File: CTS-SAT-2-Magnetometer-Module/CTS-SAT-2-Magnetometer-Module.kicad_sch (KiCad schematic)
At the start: 24 parts, among them J1 PicoBlade, J2 SWD, U1 MMC5983MA, U2 LIS2MDL, U3 STM32F072C8Tx, U4 MIC5365-3.3YD5

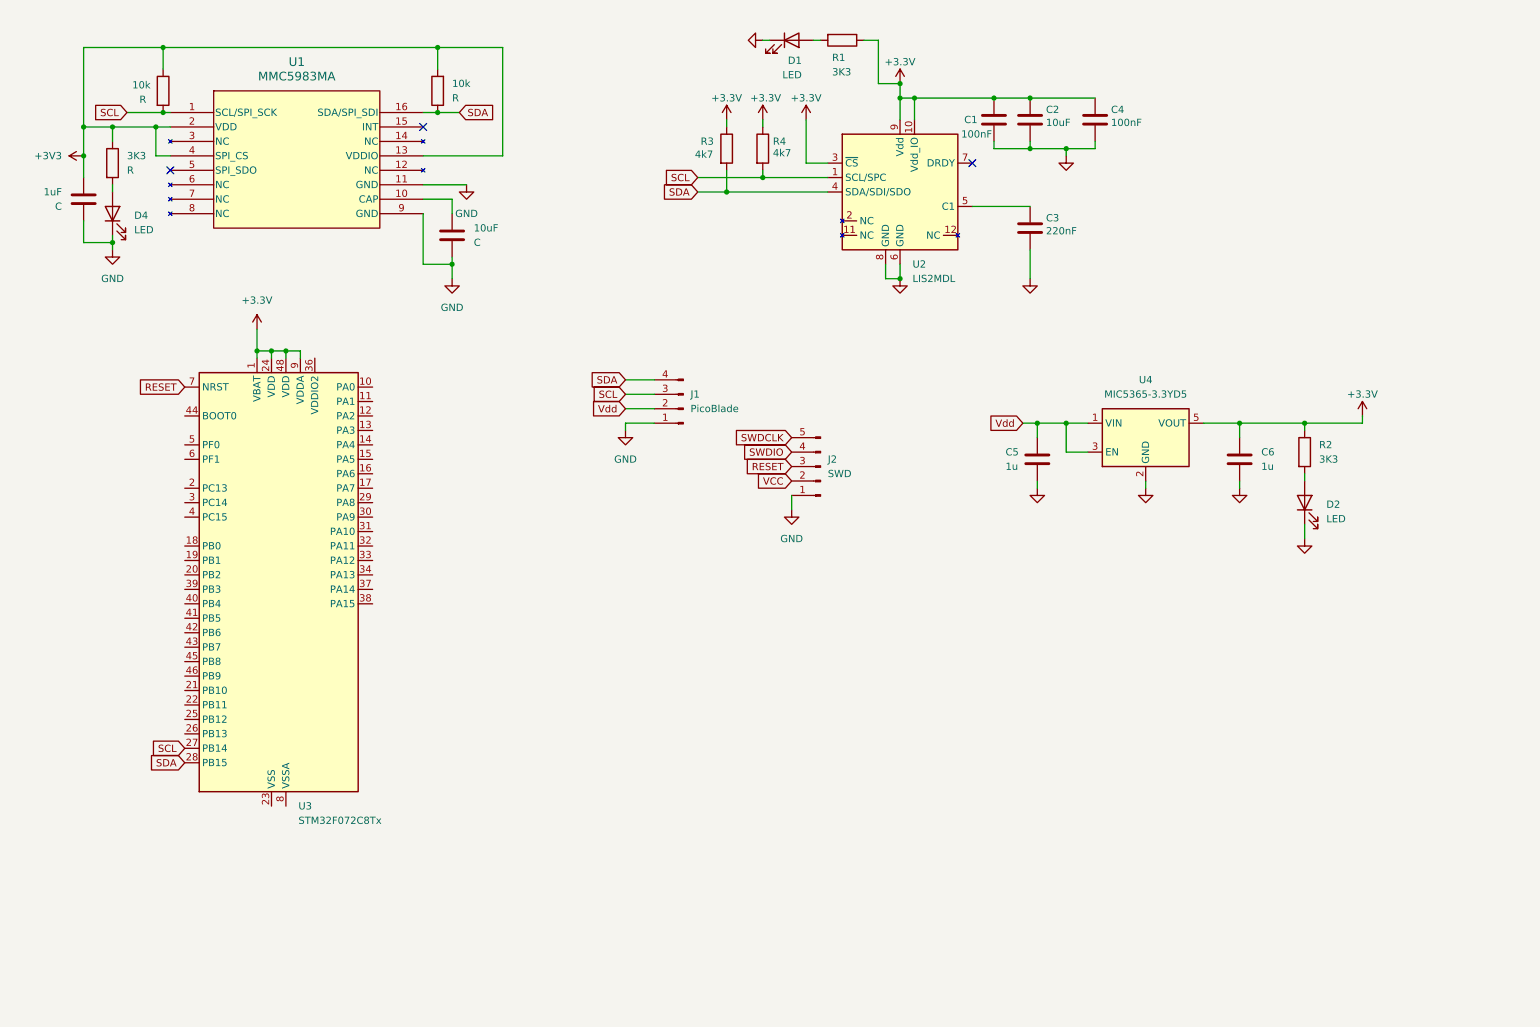
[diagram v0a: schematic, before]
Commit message: Updated Schematic and Started Layout
Assigned Footprints and Started PCB layout
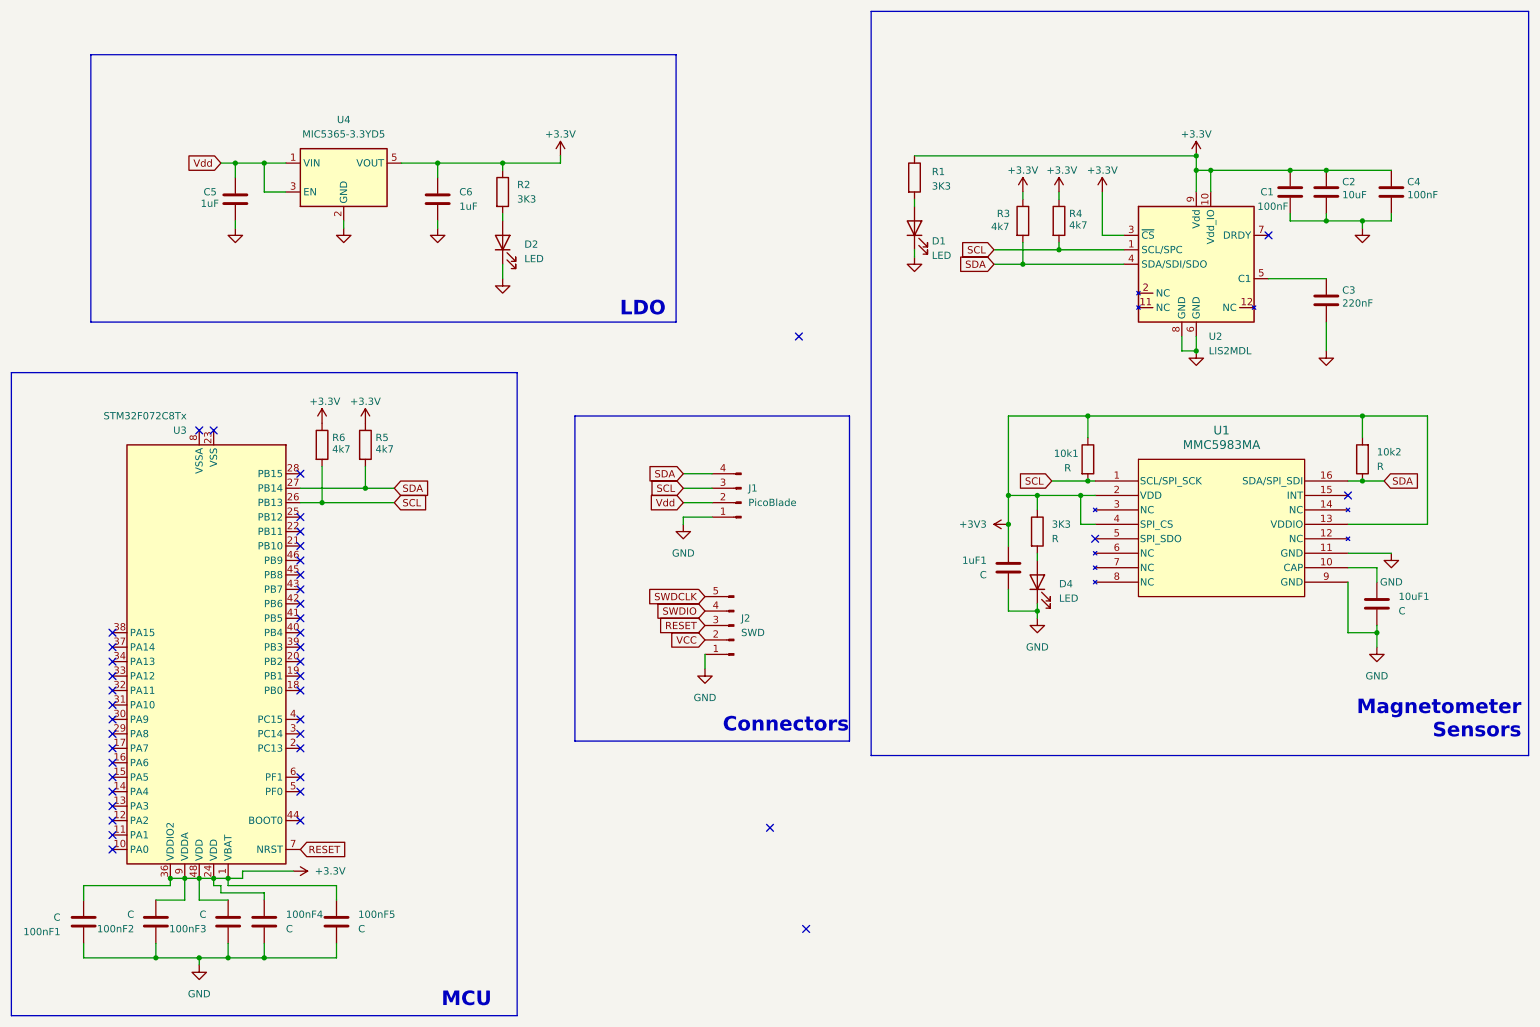
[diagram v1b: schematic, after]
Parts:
- added 100nF1, 100nF2, 100nF3, 100nF4, 100nF5: C, Capacitor_SMD:C_0603_1608Metric_Pad1.08x0.95mm_HandSolder, symbol Device:C
- added R5, R6: 4k7, Resistor_SMD:R_0603_1608Metric_Pad0.98x0.95mm_HandSolder, symbol Device:R
- 10k1, 10k2: renamed from 10k; footprint (none) -> Resistor_SMD:R_0603_1608Metric_Pad0.98x0.95mm_HandSolder
- 10uF1: renamed from 10uF; footprint (none) -> Capacitor_SMD:C_0603_1608Metric_Pad1.08x0.95mm_HandSolder
- 1uF1: renamed from 1uF; footprint (none) -> Capacitor_SMD:C_0603_1608Metric_Pad1.08x0.95mm_HandSolder
- 3K3: footprint (none) -> Resistor_SMD:R_0603_1608Metric_Pad0.98x0.95mm_HandSolder
- C5, C6: value 1u -> 1uF
- D4: footprint (none) -> LED_SMD:LED_0603_1608Metric_Pad1.05x0.95mm_HandSolder
- J2: footprint (none) -> Connector_PinSocket_2.54mm:PinSocket_1x06_P2.54mm_Vertical
- U1: footprint MMC5983MA_MEM -> 00_Footprint_Library:MMC5983MA_MEM
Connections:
- net +3.3V: now also U3.36 (VDDIO2), 100nF1.2, 100nF2.2, 100nF3.2, 100nF4.2, 100nF5.1, R5.1, R6.1
- net GND: now also 100nF1.1, 100nF2.1, 100nF3.1, 100nF4.1, 100nF5.2
- net SCL: now also U3.26 (PB13), R6.2; no longer U3.27 (PB14)
- net SDA: now also U3.27 (PB14), R5.2; no longer U3.28 (PB15)
- no-connect marks 3 -> 44
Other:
- note added: "Connectors"
- note added: "LDO"
- note added: "MCU"
- note added: "Magnetometer Sensors"
- moved on the sheet: 10k1, 10k2, 10uF1, 1uF1, 3K3, C1, C2, C3, C4, C5, C6, D1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

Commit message: Started PCB Routing
Still need to figure out how to do routing for communication lines
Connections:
- net +3V3 is gone; now on net +3.3V: 10k1.1, 10k2.2, 1uF1.1, 3K3.1, U1.13 (VDDIO), U1.2 (VDD), U1.4 (SPI_CS)
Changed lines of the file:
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@@
 	(wire
 		(pts
-			(xy 57.15 168.91) (xy 57.15 170.18)
-		)
-		(stroke
-			(width 0)
-			(type default)
-		)
-	)
-	(wire
-		(pts
 			(xy 113.03 43.18) (xy 113.03 44.45)
 		)
@@
 	(wire
 		(pts
-			(xy 66.04 168.91) (xy 57.15 168.91)
+			(xy 185.42 105.41) (xy 185.42 107.95)
 		)
 		(stroke
@@
 	(wire
 		(pts
+			(xy 185.42 107.95) (xy 191.77 107.95)
+		)
+		(stroke
+			(width 0)
+			(type default)
+		)
+	)
+	(wire
+		(pts
 			(xy 200.66 50.8) (xy 200.66 49.53)
 		)
@@
 	(wire
 		(pts
-			(xy 57.15 170.18) (xy 54.61 170.18)
+			(xy 54.61 170.18) (xy 77.47 170.18)
 		)
 		(stroke
@@
 	)
 	(symbol
+		(lib_id "power:+3.3V")
+		(at 185.42 105.41 0)
+		(unit 1)
+		(exclude_from_sim no)
+		(in_bom yes)
+		(on_board yes)
+		(dnp no)
+		(property "Reference" "#PWR01"
+			(at 185.42 109.22 0)
+			(effects
+				(font
+					(size 1.27 1.27)
+				)
+				(hide yes)
+			)
+		)
+		(property "Value" "+3.3V"
+			(at 185.42 101.6 0)
+			(effects
+				(font
+					(size 1.27 1.27)
+				)
+			)
+		)
+		(property "Footprint" ""
+			(at 185.42 105.41 0)
+			(effects
+				(font
+					(size 1.27 1.27)
+				)
+				(hide yes)
+			)
+		)
+		(property "Datasheet" ""
+			(at 185.42 105.41 0)
+			(effects
+				(font
+					(size 1.27 1.27)
+				)
+				(hide yes)
+			)
+		)
+		(property "Description" "Power symbol creates a global label with name \"+3.3V\""
+			(at 185.42 105.41 0)
+			(effects
+				(font
+					(size 1.27 1.27)
+				)
+				(hide yes)
+			)
+		)
+		(pin "1"
+		)
+		(instances
+			(project "CTS-SAT-2-Magnetometer-Module"
+				(path "/c009ac64-8176-4e92-bfe3-b763ec3b9dfb"
+					(reference "#PWR01")
+					(unit 1)
+				)
+			)
+		)
+	)
+	(symbol
 		(lib_id "power:GND")
 		(at 138.43 133.35 0)
@@
 	(symbol
 		(lib_id "power:+3.3V")
-		(at 66.04 168.91 270)
+		(at 77.47 170.18 0)
 		(unit 1)
 		(exclude_from_sim no)
@@
 		(fields_autoplaced yes)
 		(property "Reference" "#PWR027"
-			(at 62.23 168.91 0)
+			(at 77.47 173.99 0)
 			(effects
 				(font
@@
 		)
 		(property "Value" "+3.3V"
-			(at 69.85 168.9101 90)
+			(at 80.01 168.9099 0)
 			(effects
 				(font
@@
 		)
 		(property "Footprint" ""
-			(at 66.04 168.91 0)
+			(at 77.47 170.18 0)
 			(effects
 				(font
@@
 		)
 		(property "Datasheet" ""
-			(at 66.04 168.91 0)
+			(at 77.47 170.18 0)
 			(effects
 				(font
@@
 		)
 		(property "Description" "Power symbol creates a global label with name \"+3.3V\""
-			(at 66.04 168.91 0)
+			(at 77.47 170.18 0)
 			(effects
 				(font
@@
 					(unit 1)
 				)
-			)
-		)
-	)
-	(symbol
-		(lib_id "power:+3V3")
-		(at 191.77 107.95 90)
-		(unit 1)
-		(exclude_from_sim no)
-		(in_bom yes)
-		(on_board yes)
-		(dnp no)
-		(fields_autoplaced yes)
-		(property "Reference" "#PWR01"
-			(at 195.58 107.95 0)
-			(effects
-				(font
-					(size 1.27 1.27)
-				)
-				(hide yes)
-			)
-		)
-		(property "Value" "+3V3"
-			(at 187.96 107.9499 90)
-			(effects
-				(font
-					(size 1.27 1.27)
-				)
-				(justify left)
-			)
-		)
-		(property "Footprint" ""
-			(at 191.77 107.95 0)
-			(effects
-				(font
-					(size 1.27 1.27)
-				)
-				(hide yes)
-			)
-		)
-		(property "Datasheet" ""
-			(at 191.77 107.95 0)
-			(effects
-				(font
-					(size 1.27 1.27)
-				)
-				(hide yes)
-			)
-		)
-		(property "Description" "Power symbol creates a global label with name \"+3V3\""
-			(at 191.77 107.95 0)
-			(effects
-				(font
-					(size 1.27 1.27)
-				)
-				(hide yes)
-			)
-		)
-		(pin "1"
-		)
-		(instances
-			(project ""
-				(path "/c009ac64-8176-4e92-bfe3-b763ec3b9dfb"
-					(reference "#PWR01")
-					(unit 1)
-				)

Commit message: Changed one of the footprints
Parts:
- J2: footprint Connector_PinSocket_2.54mm:PinSocket_1x06_P2.54mm_Vertical -> Connector_PinSocket_2.54mm:PinSocket_1x05_P2.54mm_Vertical
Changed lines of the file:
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@@
 			)
 		)
-		(property "Footprint" "Connector_PinSocket_2.54mm:PinSocket_1x06_P2.54mm_Vertical"
+		(property "Footprint" "Connector_PinSocket_2.54mm:PinSocket_1x05_P2.54mm_Vertical"
 			(at 143.51 125.73 0)
 			(effects

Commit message: Few first edits
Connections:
- net VCC is gone; now on net Vdd: J2.2 (Pin_2)
- net +3.3V: no longer 10k1.1, 10k2.2, 1uF1.1, 3K3.1, U1.13 (VDDIO), U1.2 (VDD), U1.4 (SPI_CS)
- new net +3V0: 10k1.1, 10k2.2, 1uF1.1, 3K3.1, U1.13 (VDDIO), U1.2 (VDD), U1.4 (SPI_CS)

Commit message: Aaryan's Changes applied
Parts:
- removed 10k1, 10k2, 3K3: R, Resistor_SMD:R_0603_1608Metric_Pad0.98x0.95mm_HandSolder, symbol Device:R
- removed D1: LED, LED_SMD:LED_0603_1608Metric_Pad1.05x0.95mm_HandSolder, symbol Device:LED
- added C7: 100nF, symbol Device:C
- added D3: LED, LED_SMD:LED_0603_1608Metric_Pad1.05x0.95mm_HandSolder, symbol Device:LED
- added R7: 3K3, Resistor_SMD:R_0603_1608Metric_Pad0.98x0.95mm_HandSolder, symbol Device:R
- added SW1: SW_Push, symbol Switch:SW_Push
- C: renamed from 100nF3; value C -> 100nF3
- C: renamed from 100nF4; value C -> 100nF4
- C: renamed from 100nF1; value C -> 100nF1
- C: renamed from 100nF5; value C -> 100nF5
- C: renamed from 10uF1; value C -> 10uF1
- C: renamed from 100nF2; value C -> 100nF2
- C: renamed from 1uF1; value C -> 1uF1
- R1: value 3K3 -> 0; footprint Resistor_SMD:R_0603_1608Metric_Pad0.98x0.95mm_HandSolder -> (none)
- R3: value 4k7 -> 10k; footprint Resistor_SMD:R_0603_1608Metric_Pad0.98x0.95mm_HandSolder -> (none)
- R4: value 4k7 -> 3K3
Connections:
- net +3V0: now also C.1, C.2, C.2, C.2, C.2, C1.2, C2.1, C4.1, C6.1, R1.1, R2.1, R3.1, R5.1, R6.1, U2.10 (Vdd_IO), U2.9 (Vdd), U3.1 (VBAT), U3.24 (VDD), U3.36 (VDDIO2), U3.48 (VDD), U3.9 (VDDA), U4.5 (VOUT)
- net GND: now also U3.23 (VSS), U3.35 (VSS), U3.47 (VSS), U3.8 (VSSA), C7.2, D3.1 (K), SW1.2
- net SCL: no longer R4.2
- net SDA: no longer R3.2
- net SWDCLK: now also U3.37 (PA14)
- net SWDIO: now also U3.34 (PA13)
- net at U3.18 (PB0): now also R4.1
- net at U3.19 (PB1): now also R7.1
- net DRDY: now reaches U3.21 (PB10)
- net DRDY: now also U2.7 (DRDY)
- net at R1.2: now also U2.3 (~{CS})
- net at D4.2 (A): now also R7.2
- removed net +3.3V: C.1, C.2, C.2, C.2, C.2, C1.2, C2.1, C4.1, C6.1, R1.1, R2.1, R3.1, R4.1, R5.1, R6.1, U2.10 (Vdd_IO), U2.3 (~{CS}), U2.9 (Vdd), U3.1 (VBAT), U3.24 (VDD), U3.36 (VDDIO2), U3.48 (VDD), U3.9 (VDDA), U4.5 (VOUT)
- net RESET renamed NRST
- net NRST: now also R3.2, C7.1, SW1.1
- new net: D3.2 (A), R4.2
- no-connect marks 44 -> 33
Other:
- moved on the sheet: C, C5, C6, D2, R2, R5, R6, U3, U4

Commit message: Final changes for Aaryan
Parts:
- removed J1: PicoBlade, Connector_PinHeader_2.54mm:PinHeader_1x04_P2.54mm_Vertical, symbol Connector:Conn_01x04_Pin
- added J3: SWD, Connector_PinHeader_2.54mm:PinHeader_1x05_P2.54mm_Vertical, symbol Connector:Conn_01x05_Pin
- C7: footprint (none) -> Capacitor_SMD:C_0603_1608Metric_Pad1.08x0.95mm_HandSolder
- R1, R3: footprint (none) -> Resistor_SMD:R_0603_1608Metric_Pad0.98x0.95mm_HandSolder
- SW1: footprint (none) -> Button_Switch_SMD:SW_SPST_EVQP0
- renumbered C to C10, C to C11, C to C12, C to C13, C to C14, C to C8, C to C9
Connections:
- net GND: now also J3.1 (Pin_1)
- net NRST: now also J3.3 (Pin_3)
- net SWDCLK: now also J3.5 (Pin_5)
- net SWDIO: now also J3.4 (Pin_4)
- net Vdd: now also J3.2 (Pin_2)
- net INT: now reaches U3.20 (PB2)
- net INT: now also U1.15 (INT)
- no-connect marks 33 -> 31
